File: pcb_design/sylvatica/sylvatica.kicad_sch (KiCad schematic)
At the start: 121 parts, among them J1 USB_C_Receptacle, J2 USB_C_Receptacle, J3 USB_C_Receptacle, J4 USB_C_Receptacle, J5 Conn_02x07_Odd_Even, J6 Conn_02x07_Odd_Even, J9 Conn_01x06_Female, Q1 Q_NMOS_GSD, Q2 Q_NMOS_GSD, SW1 SW_Push, U1 PGA113, U10 dsPIC33EP512MC806, U11 SiP32431, U12 LP2985-5.0, U13 REF2033, U14 OPA320, U15 SiP32431, U16 SiP32431, U17 SiP32431, U18 SiP32431, U19 ADM7170, U2 PGA113, U20 MCP2542FD, U21 TPS737, U22 SiP32431, U3 PGA113, U4 PGA113, U5 PGA113, U6 PGA113, U7 PGA113, U8 PGA113, U9 ADS8332, Y1 Crystal_GND24

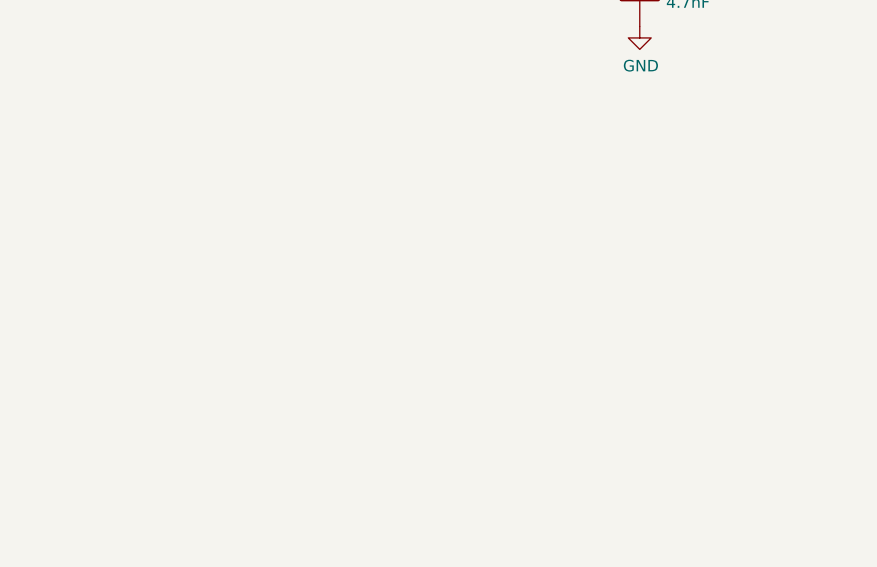
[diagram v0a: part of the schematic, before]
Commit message: Minor improvements.
Mostly related to external pull-ups of 10k for I2C
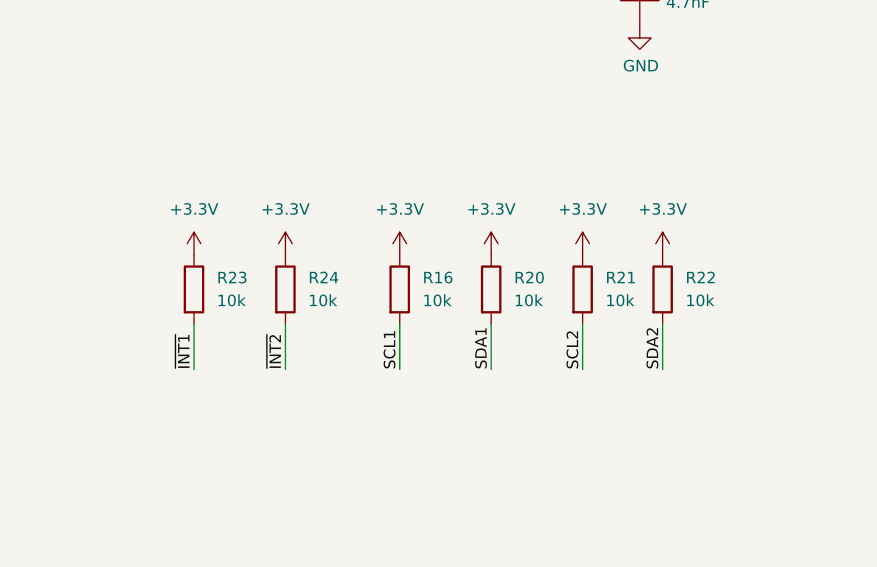
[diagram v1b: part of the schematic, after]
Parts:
- added R16, R20, R21, R22, R23, R24: 10k, Resistor_SMD:R_0603_1608Metric, symbol Device:R
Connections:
- net +3.3V: now also R16.1, R20.1, R21.1, R22.1, R23.1, R24.1
- net SCL1: now also R16.2
- net SCL2: now also R21.2
- net SDA1: now also R20.2
- net SDA2: now also R22.2
- net ~{INT1}: now also R23.2
- net ~{INT2}: now also R24.2

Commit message: Fix net issue.
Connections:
- net +5V is gone; now on net VBUS: C9.1, R10.1, U12.1 (VIN)
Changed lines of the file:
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@@
     (stroke (width 0) (type default) (color 0 0 0 0))
   )
-  (wire (pts (xy 212.09 256.54) (xy 212.09 260.35))
-    (stroke (width 0) (type default) (color 0 0 0 0))
-  )
   (wire (pts (xy 360.68 210.82) (xy 354.33 210.82))
     (stroke (width 0) (type default) (color 0 0 0 0))
@@
     (pin "1")
   )
-  (symbol (lib_id "power:+5V") (at 207.01 222.25 0) (unit 1)
-    (in_bom yes) (on_board yes)
-    (property "Reference" "#PWR038" (id 0) (at 207.01 226.06 0)
-      (effects (font (size 1.27 1.27)) hide)
-    )
-    (property "Value" "+5V" (id 1) (at 207.391 217.8558 0))
-    (property "Footprint" "" (id 2) (at 207.01 222.25 0)
-      (effects (font (size 1.27 1.27)) hide)
-    )
-    (property "Datasheet" "" (id 3) (at 207.01 222.25 0)
-      (effects (font (size 1.27 1.27)) hide)
-    )
-    (pin "1")
-  )
   (symbol (lib_id "Device:Q_NMOS_GSD") (at 264.16 267.97 270) (unit 1)
     (in_bom yes) (on_board yes)
@@
     (pin "1")
   )
-  (symbol (lib_id "power:+5V") (at 274.32 255.27 0) (unit 1)
-    (in_bom yes) (on_board yes)
-    (property "Reference" "#PWR046" (id 0) (at 274.32 259.08 0)
-      (effects (font (size 1.27 1.27)) hide)
-    )
-    (property "Value" "+5V" (id 1) (at 274.701 250.8758 0))
-    (property "Footprint" "" (id 2) (at 274.32 255.27 0)
-      (effects (font (size 1.27 1.27)) hide)
-    )
-    (property "Datasheet" "" (id 3) (at 274.32 255.27 0)
-      (effects (font (size 1.27 1.27)) hide)
-    )
-    (pin "1")
-  )
   (symbol (lib_id "Device:C") (at 243.84 229.87 0) (unit 1)
     (in_bom yes) (on_board yes)
@@
     (pin "1")
   )
-  (symbol (lib_id "power:+5V") (at 212.09 256.54 0) (unit 1)
-    (in_bom yes) (on_board yes)
-    (property "Reference" "#PWR0120" (id 0) (at 212.09 260.35 0)
-      (effects (font (size 1.27 1.27)) hide)
-    )
-    (property "Value" "+5V" (id 1) (at 212.471 252.1458 0))
-    (property "Footprint" "" (id 2) (at 212.09 256.54 0)
-      (effects (font (size 1.27 1.27)) hide)
-    )
-    (property "Datasheet" "" (id 3) (at 212.09 256.54 0)
-      (effects (font (size 1.27 1.27)) hide)
-    )
-    (pin "1")
-  )
-  (symbol (lib_id "power:PWR_FLAG") (at 212.09 260.35 180) (unit 1)
-    (in_bom yes) (on_board yes)
-    (property "Reference" "#FLG0102" (id 0) (at 212.09 262.255 0)
-      (effects (font (size 1.27 1.27)) hide)
-    )
-    (property "Value" "PWR_FLAG" (id 1) (at 212.09 264.7442 0))
-    (property "Footprint" "" (id 2) (at 212.09 260.35 0)
-      (effects (font (size 1.27 1.27)) hide)
-    )
-    (property "Datasheet" "~" (id 3) (at 212.09 260.35 0)
-      (effects (font (size 1.27 1.27)) hide)
-    )
-    (pin "1")
-  )
   (symbol (lib_id "power:GND") (at 226.06 27.94 0) (unit 1)
     (in_bom yes) (on_board yes)
@@
     (pin "3")
   )
+  (symbol (lib_id "power:VBUS") (at 207.01 222.25 0) (unit 1)
+    (in_bom yes) (on_board yes)
+    (property "Reference" "#PWR0170" (id 0) (at 207.01 226.06 0)
+      (effects (font (size 1.27 1.27)) hide)
+    )
+    (property "Value" "VBUS" (id 1) (at 207.391 217.8558 0))
+    (property "Footprint" "" (id 2) (at 207.01 222.25 0)
+      (effects (font (size 1.27 1.27)) hide)
+    )
+    (property "Datasheet" "" (id 3) (at 207.01 222.25 0)
+      (effects (font (size 1.27 1.27)) hide)
+    )
+    (pin "1")
+  )
   (symbol (lib_id "power:+3.3V") (at 477.52 217.17 0) (unit 1)
     (in_bom yes) (on_board yes) (fields_autoplaced)
@@
     (pin "1")
   )
+  (symbol (lib_id "power:VBUS") (at 274.32 255.27 0) (unit 1)
+    (in_bom yes) (on_board yes)
+    (property "Reference" "#PWR0120" (id 0) (at 274.32 259.08 0)
+      (effects (font (size 1.27 1.27)) hide)
+    )
+    (property "Value" "VBUS" (id 1) (at 274.701 250.8758 0))
+    (property "Footprint" "" (id 2) (at 274.32 255.27 0)
+      (effects (font (size 1.27 1.27)) hide)
+    )
+    (property "Datasheet" "" (id 3) (at 274.32 255.27 0)
+      (effects (font (size 1.27 1.27)) hide)
+    )
+    (pin "1")
+  )
   (symbol (lib_id "Device:R") (at 519.43 220.98 0) (unit 1)
     (in_bom yes) (on_board yes) (fields_autoplaced)
@@
       (reference "#FLG0101") (unit 1) (value "PWR_FLAG") (footprint "")
     )
-    (path "/00000000-0000-0000-0000-00005c39af2e"
-      (reference "#FLG0102") (unit 1) (value "PWR_FLAG") (footprint "")
-    )
     (path "/00000000-0000-0000-0000-00005c43c7c5"
       (reference "#FLG0104") (unit 1) (value "PWR_FLAG") (footprint "")
@@
       (reference "#PWR037") (unit 1) (value "GND") (footprint "")
     )
-    (path "/00000000-0000-0000-0000-00005c1ad482"
-      (reference "#PWR038") (unit 1) (value "+5V") (footprint "")
-    )
     (path "/00000000-0000-0000-0000-00005ded0e83"
       (reference "#PWR039") (unit 1) (value "GND") (footprint "")
@@
       (reference "#PWR045") (unit 1) (value "GND") (footprint "")
     )
-    (path "/00000000-0000-0000-0000-00005c1d7080"
-      (reference "#PWR046") (unit 1) (value "+5V") (footprint "")
-    )
     (path "/8a1ccef6-15c1-40ff-bcfa-a6af3a8ffcde"
       (reference "#PWR047") (unit 1) (value "GND") (footprint "")
@@
       (reference "#PWR0119") (unit 1) (value "GND") (footprint "")
     )
-    (path "/00000000-0000-0000-0000-00005c39a91e"
-      (reference "#PWR0120") (unit 1) (value "+5V") (footprint "")
+    (path "/9b680d0e-851b-40ae-8644-ae3a5e70b721"
+      (reference "#PWR0120") (unit 1) (value "VBUS") (footprint "")
     )
     (path "/00000000-0000-0000-0000-00005ca06edd"
@@
       (reference "#PWR0169") (unit 1) (value "+3.3V") (footprint "")
     )
+    (path "/30070e40-14c3-45d7-99c7-39484c2df104"
+      (reference "#PWR0170") (unit 1) (value "VBUS") (footprint "")
+    )
     (path "/00000000-0000-0000-0000-00005c38abcd"

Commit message: Various updates for Aisler order.
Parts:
- C60: Mouser (none) -> 791-1206X225K250CT
- U11, U16, U17, U18: Mouser (none) -> 781-SIP32431DR3-GE3; Price (none) -> 0.41
- U19: Mouser (none) -> ADM7170ACPZ-3.3-R7
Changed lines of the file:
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@@
+      (effects (font (size 1.27 1.27)) hide)
+    )
+    (property "Mouser" "781-SIP32431DR3-GE3" (id 4) (at 414.02 285.75 0)
+      (effects (font (size 1.27 1.27)) hide)
+    )
+    (property "Price" "0.41" (id 5) (at 414.02 285.75 0)
       (effects (font (size 1.27 1.27)) hide)
     )
@@
       (effects (font (size 1.27 1.27)) hide)
     )
+    (property "Mouser" "781-SIP32431DR3-GE3" (id 4) (at 414.02 311.15 0)
+      (effects (font (size 1.27 1.27)) hide)
+    )
+    (property "Price" "0.41" (id 5) (at 414.02 311.15 0)
+      (effects (font (size 1.27 1.27)) hide)
+    )
     (pin "1")
     (pin "2")
@@
       (effects (font (size 1.27 1.27)) hide)
     )
+    (property "Mouser" "791-1206X225K250CT" (id 4) (at 417.83 39.37 0)
+      (effects (font (size 1.27 1.27)) hide)
+    )
     (pin "1")
     (pin "2")
@@
     )
     (property "Datasheet" "" (id 3) (at 497.84 44.45 0)
+      (effects (font (size 1.27 1.27)) hide)
+    )
+    (property "Mouser" "ADM7170ACPZ-3.3-R7" (id 4) (at 497.84 44.45 0)
       (effects (font (size 1.27 1.27)) hide)
     )
@@
       (effects (font (size 1.27 1.27)) hide)
     )
+    (property "Mouser" "781-SIP32431DR3-GE3" (id 4) (at 414.02 335.28 0)
+      (effects (font (size 1.27 1.27)) hide)
+    )
+    (property "Price" "0.41" (id 5) (at 414.02 335.28 0)
+      (effects (font (size 1.27 1.27)) hide)
+    )
     (pin "1")
     (pin "2")
@@
       (effects (font (size 1.27 1.27)) hide)
     )
+    (property "Mouser" "781-SIP32431DR3-GE3" (id 4) (at 414.02 360.68 0)
+      (effects (font (size 1.27 1.27)) hide)
+    )
+    (property "Price" "0.41" (id 5) (at 414.02 360.68 0)
+      (effects (font (size 1.27 1.27)) hide)
+    )
